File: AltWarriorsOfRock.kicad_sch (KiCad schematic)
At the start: 17 parts, among them J1 Fret Board, J2 South Inputs

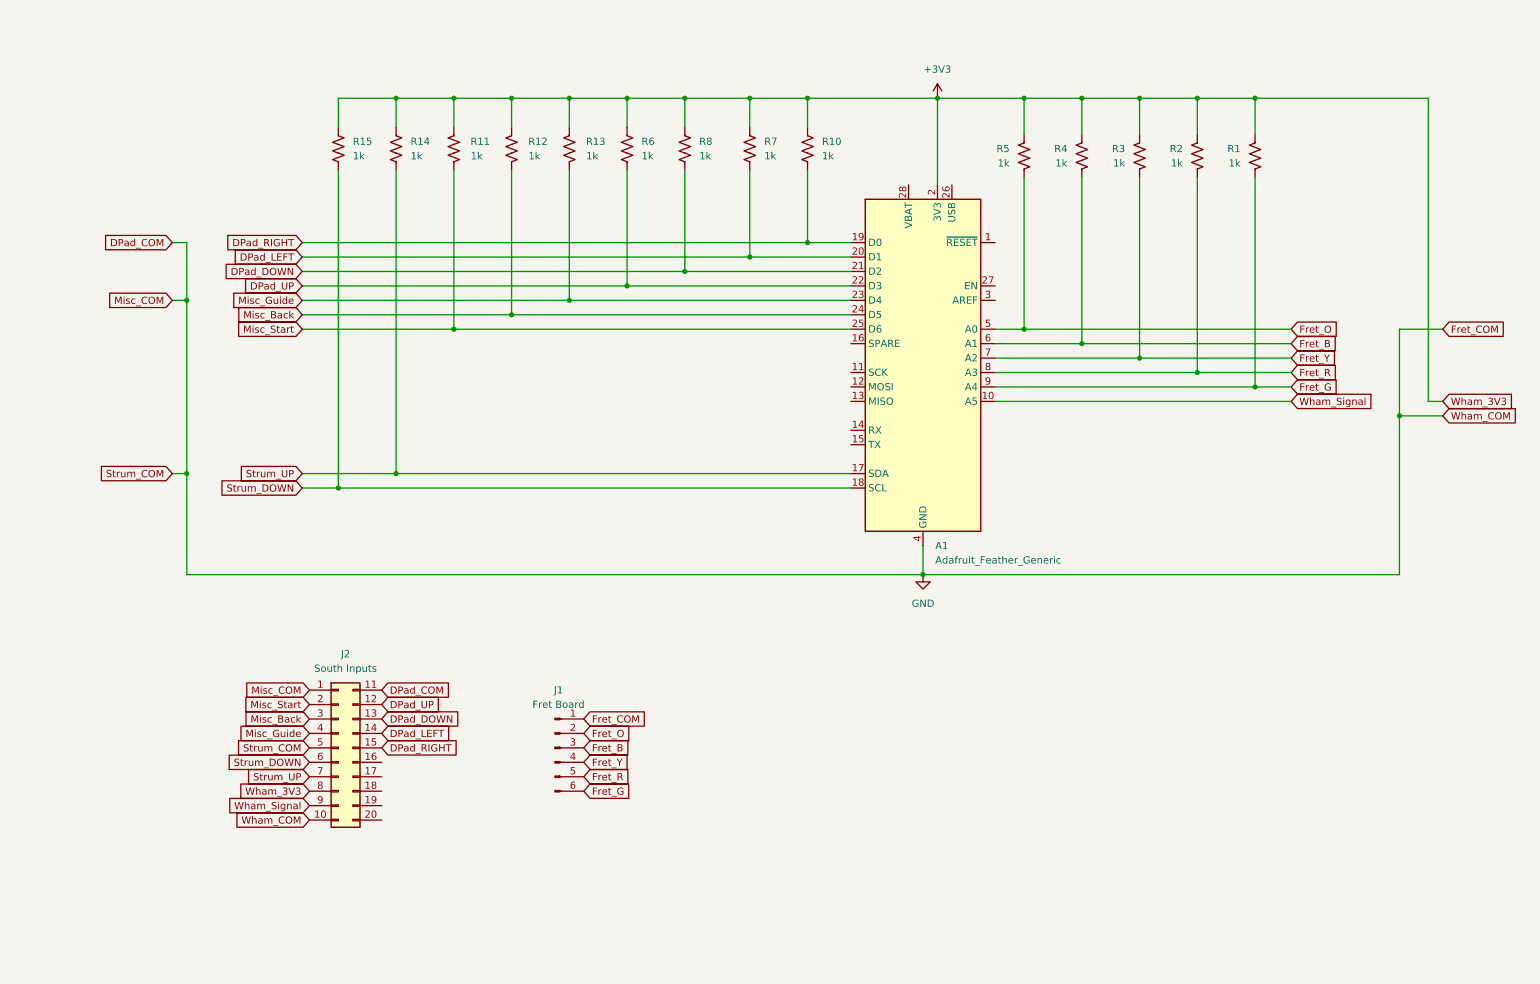
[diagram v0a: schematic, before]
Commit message: Switch to ESP32-S3-WROOM-1 module; Use 5.1k for all pullups
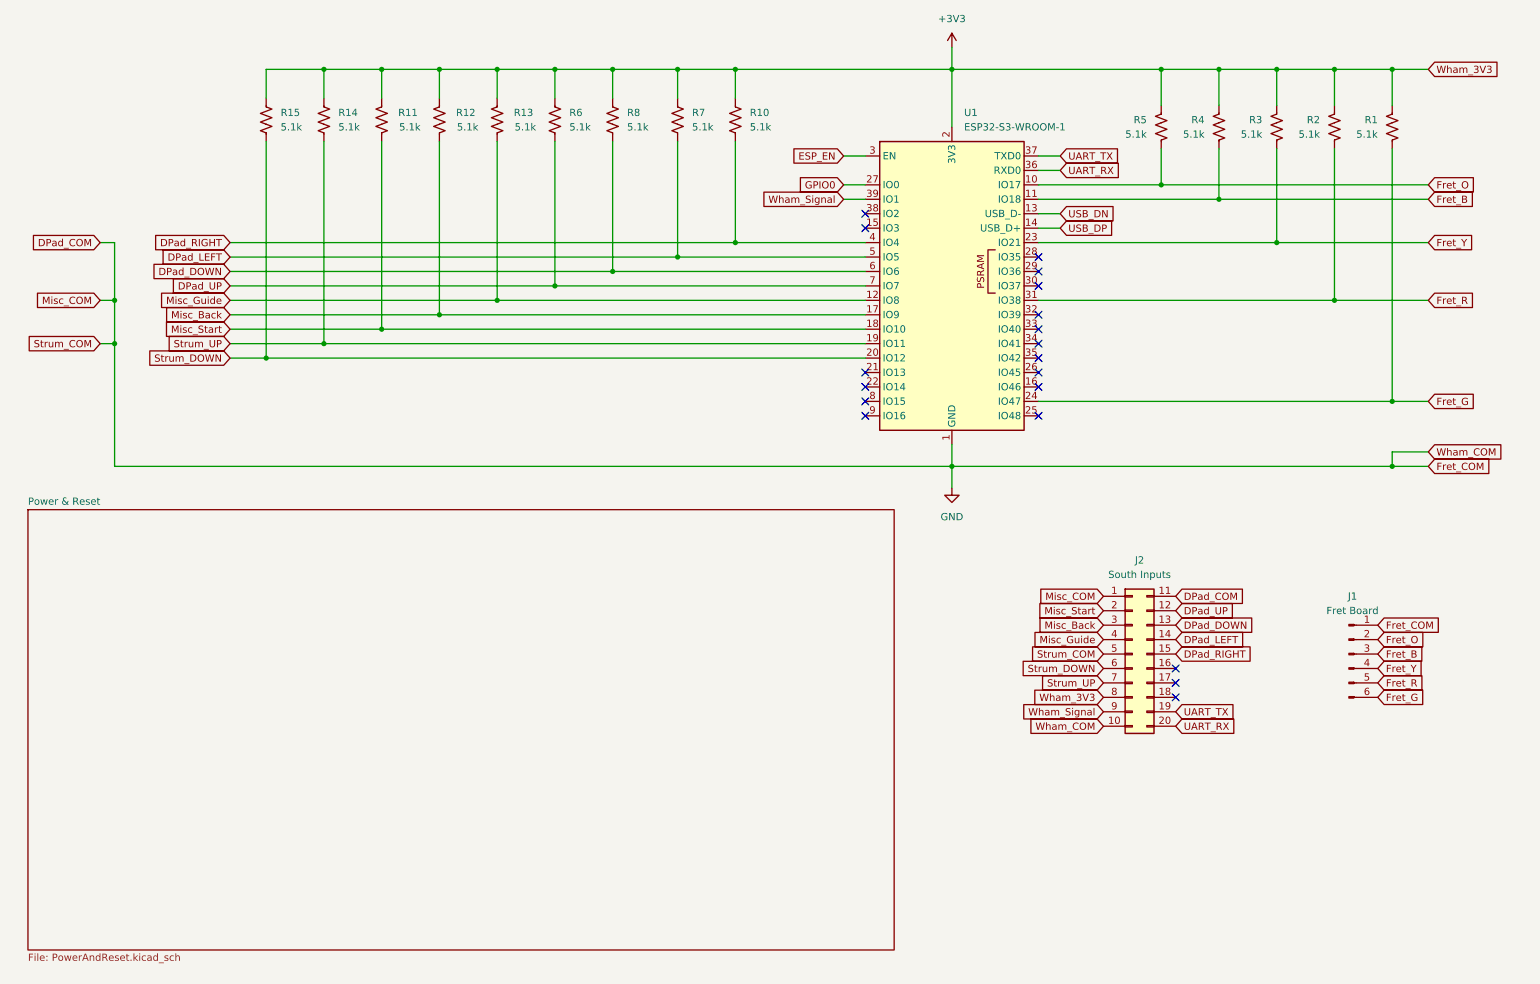
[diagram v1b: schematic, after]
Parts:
- removed A1: Adafruit_Feather_Generic, Module:Adafruit_Feather, symbol MCU_Module:Adafruit_Feather_Generic
- added U1: ESP32-S3-WROOM-1, RF_Module:ESP32-S3-WROOM-1, symbol RF_Module:ESP32-S3-WROOM-1
- R1, R10, R11, R12, R13, R14, R15, R2, R3, R4, R5, R6, R7, R8: value 1k -> 5.1k; footprint Resistor_THT:R_Axial_DIN0204_L3.6mm_D1.6mm_P7.62mm_Horizontal -> Resistor_SMD:R_1206_3216Metric_Pad1.30x1.75mm_HandSolder
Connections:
- net +3V3: now also U1.2 (3V3)
- net DPad_DOWN: now also U1.6 (IO6)
- net DPad_LEFT: now also U1.5 (IO5)
- net DPad_RIGHT: now also U1.4 (IO4)
- net DPad_UP: now also U1.7 (IO7)
- net Fret_B: now also U1.11 (IO18)
- net Fret_G: now also U1.24 (IO47)
- net Fret_O: now also U1.10 (IO17)
- net Fret_R: now also U1.31 (IO38)
- net Fret_Y: now also U1.23 (IO21)
- net GND: now also U1.1 (GND), U1.40 (GND), U1.41 (GND)
- net Misc_Back: now also U1.17 (IO9)
- net Misc_Guide: now also U1.12 (IO8)
- net Misc_Start: now also U1.18 (IO10)
- net Strum_DOWN: now also U1.20 (IO12)
- net Strum_UP: now also U1.19 (IO11)
- net Wham_Signal: now also U1.39 (IO1)
- net UART_TX: now reaches J2.19 (Pin_19)
- net UART_TX: now also U1.37 (TXD0)
- net UART_RX: now reaches J2.20 (Pin_20)
- net UART_RX: now also U1.36 (RXD0)
- new net ESP_EN: U1.3 (EN)
- new net GPIO0: U1.27 (IO0)
- new net USB_DN: U1.13 (USB_D-)
- new net USB_DP: U1.14 (USB_D+)
- no-connect marks 0 -> 19
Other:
- added sheet Power & Reset (PowerAndReset.kicad_sch)
- moved on the sheet: J1, J2, R1, R10, R11, R12, R13, R14, R15, R2, R3, R4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

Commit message: Draft 01 of PCB with WROOM module
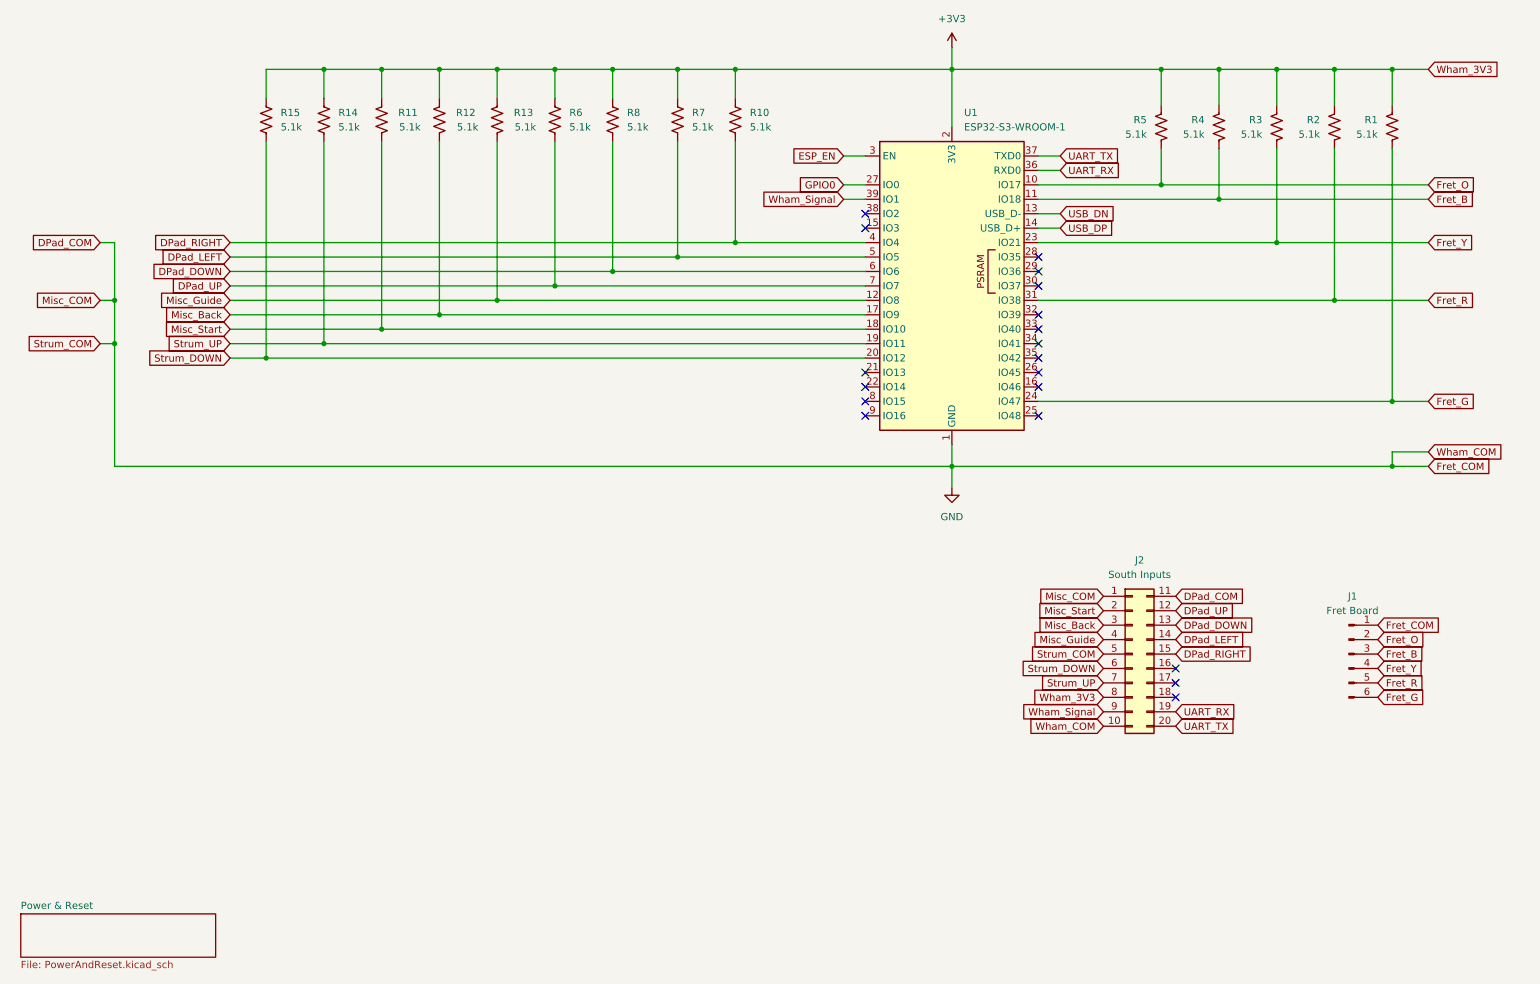
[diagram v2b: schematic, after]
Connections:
- net UART_RX: now also J2.19 (Pin_19); no longer J2.20 (Pin_20)
- net UART_TX: now also J2.20 (Pin_20); no longer J2.19 (Pin_19)
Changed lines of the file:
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@@
 	(global_label "UART_RX"
 		(shape input)
+		(at 219.71 148.59 0)
+		(fields_autoplaced yes)
+		(effects
+			(font
+				(size 1.27 1.27)
+			)
+			(justify left)
+		)
+		(property "Intersheetrefs" "${INTERSHEET_REFS}"
+			(at 230.799 148.59 0)
+			(effects
+				(font
+					(size 1.27 1.27)
+				)
+				(justify left)
+				(hide yes)
+			)
+		)
+	)
+	(global_label "DPad_RIGHT"
+		(shape input)
+		(at 53.34 66.04 180)
+		(fields_autoplaced yes)
+		(effects
+			(font
+				(size 1.27 1.27)
+			)
+			(justify right)
+		)
+		(property "Intersheetrefs" "${INTERSHEET_REFS}"
+			(at 39.1063 66.04 0)
+			(effects
+				(font
+					(size 1.27 1.27)
+				)
+				(justify right)
+				(hide yes)
+			)
+		)
+	)
+	(global_label "Fret_B"
+		(shape input)
+		(at 264.16 58.42 0)
+		(fields_autoplaced yes)
+		(effects
+			(font
+				(size 1.27 1.27)
+			)
+			(justify left)
+		)
+		(property "Intersheetrefs" "${INTERSHEET_REFS}"
+			(at 273.0719 58.42 0)
+			(effects
+				(font
+					(size 1.27 1.27)
+				)
+				(justify left)
+				(hide yes)
+			)
+		)
+	)
+	(global_label "Fret_G"
+		(shape input)
+		(at 255.27 146.05 0)
+		(fields_autoplaced yes)
+		(effects
+			(font
+				(size 1.27 1.27)
+			)
+			(justify left)
+		)
+		(property "Intersheetrefs" "${INTERSHEET_REFS}"
+			(at 264.1819 146.05 0)
+			(effects
+				(font
+					(size 1.27 1.27)
+				)
+				(justify left)
+				(hide yes)
+			)
+		)
+	)
+	(global_label "UART_TX"
+		(shape input)
 		(at 219.71 151.13 0)
 		(fields_autoplaced yes)
@@
 		)
 		(property "Intersheetrefs" "${INTERSHEET_REFS}"
-			(at 230.799 151.13 0)
-			(effects
-				(font
-					(size 1.27 1.27)
-				)
-				(justify left)
-				(hide yes)
-			)
-		)
-	)
-	(global_label "DPad_RIGHT"
-		(shape input)
-		(at 53.34 66.04 180)
-		(fields_autoplaced yes)
-		(effects
-			(font
-				(size 1.27 1.27)
-			)
-			(justify right)
-		)
-		(property "Intersheetrefs" "${INTERSHEET_REFS}"
-			(at 39.1063 66.04 0)
-			(effects
-				(font
-					(size 1.27 1.27)
-				)
-				(justify right)
-				(hide yes)
-			)
-		)
-	)
-	(global_label "Fret_B"
-		(shape input)
-		(at 264.16 58.42 0)
-		(fields_autoplaced yes)
-		(effects
-			(font
-				(size 1.27 1.27)
-			)
-			(justify left)
-		)
-		(property "Intersheetrefs" "${INTERSHEET_REFS}"
-			(at 273.0719 58.42 0)
-			(effects
-				(font
-					(size 1.27 1.27)
-				)
-				(justify left)
-				(hide yes)
-			)
-		)
-	)
-	(global_label "Fret_G"
-		(shape input)
-		(at 255.27 146.05 0)
-		(fields_autoplaced yes)
-		(effects
-			(font
-				(size 1.27 1.27)
-			)
-			(justify left)
-		)
-		(property "Intersheetrefs" "${INTERSHEET_REFS}"
-			(at 264.1819 146.05 0)
-			(effects
-				(font
-					(size 1.27 1.27)
-				)
-				(justify left)
-				(hide yes)
-			)
-		)
-	)
-	(global_label "UART_TX"
-		(shape input)
-		(at 219.71 148.59 0)
-		(fields_autoplaced yes)
-		(effects
-			(font
-				(size 1.27 1.27)
-			)
-			(justify left)
-		)
-		(property "Intersheetrefs" "${INTERSHEET_REFS}"
-			(at 230.4966 148.59 0)
+			(at 230.4966 151.13 0)
 			(effects
 				(font
@@
 	)
 	(sheet
-		(at 17.78 113.03)
-		(size 152.4 77.47)
+		(at 16.51 184.15)
+		(size 34.29 7.62)
 		(exclude_from_sim no)
 		(in_bom yes)
@@
 		)
 		(property "Sheetname" "Power & Reset"
-			(at 17.78 112.3184 0)
+			(at 16.51 183.4384 0)
 			(effects
 				(font
@@
 		)
 		(property "Sheetfile" "PowerAndReset.kicad_sch"
-			(at 17.78 191.0846 0)
-			(effects
-				(font
+			(at 16.51 192.3546 0)
+			(effects
+				(font

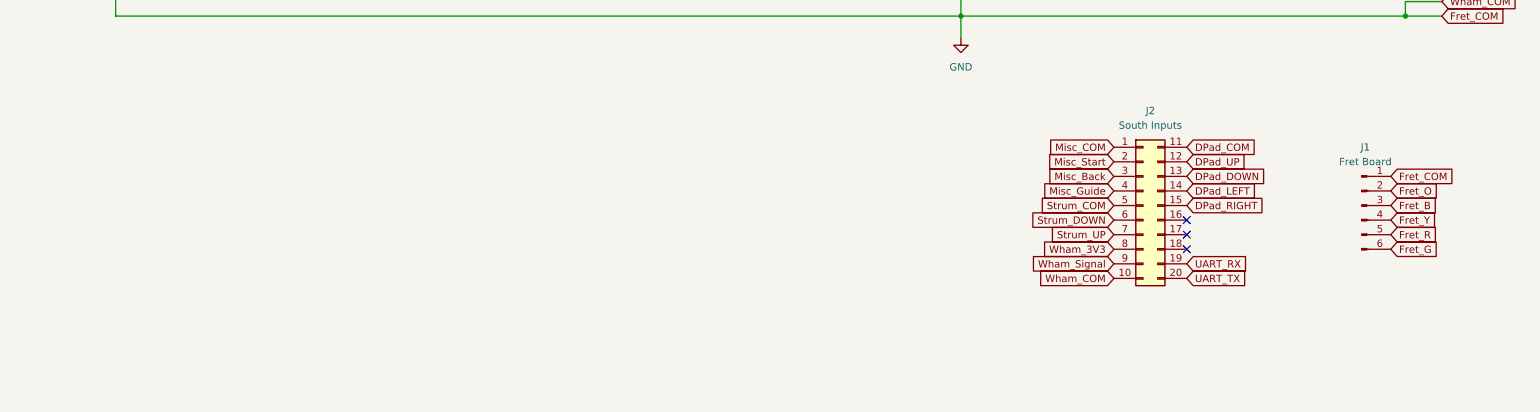
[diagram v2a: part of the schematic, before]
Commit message: [WIP] Use surface-mount headers for south headers
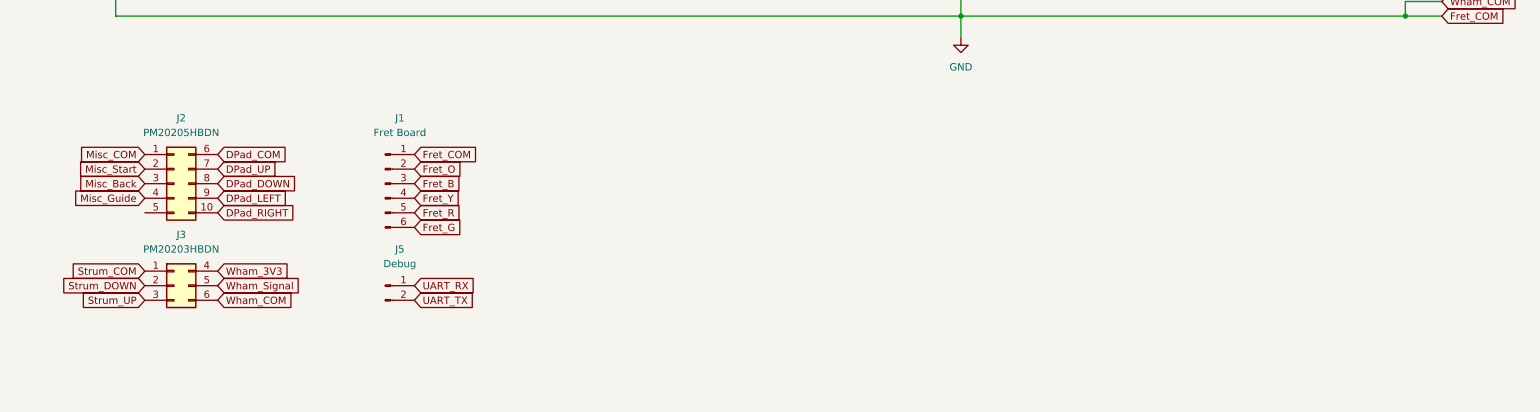
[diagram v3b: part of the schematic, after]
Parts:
- removed J2: South Inputs, Library_ygaskh:PinHeader_2x10_P2.54mm_Vertical_TopBottom, symbol Connector_Generic:Conn_02x10_Top_Bottom
- added J2: PM20205HBDN, Connector_Metz_ygaskh:PM20205HBDN, symbol Connector_Metz:PM20205HBDN
- added J3: PM20203HBDN, Connector_Metz_ygaskh:PM20203HBDN, symbol Connector_Metz:PM20203HBDN
- added J5: Debug, Connector_PinHeader_2.54mm:PinHeader_1x02_P2.54mm_Vertical, symbol Connector:Conn_01x02_Pin
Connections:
- net +3V3: now also J3.4 (Pin_4)
- net DPad_DOWN: now also J2.8 (Pin_8)
- net DPad_LEFT: now also J2.9 (Pin_9)
- net DPad_RIGHT: now also J2.10 (Pin_10)
- net DPad_UP: now also J2.7 (Pin_7)
- net GND: now also J2.1 (Pin_1), J2.6 (Pin_6), J3.1 (Pin_1), J3.6 (Pin_6)
- net Misc_Back: now also J2.3 (Pin_3)
- net Misc_Guide: now also J2.4 (Pin_4)
- net Misc_Start: now also J2.2 (Pin_2)
- net Strum_DOWN: now also J3.2 (Pin_2)
- net Strum_UP: now also J3.3 (Pin_3)
- net UART_RX: now also J5.1 (Pin_1)
- net UART_TX: now also J5.2 (Pin_2)
- net Wham_Signal: now also J3.5 (Pin_5)
- no-connect marks 19 -> 16
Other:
- moved on the sheet: J1

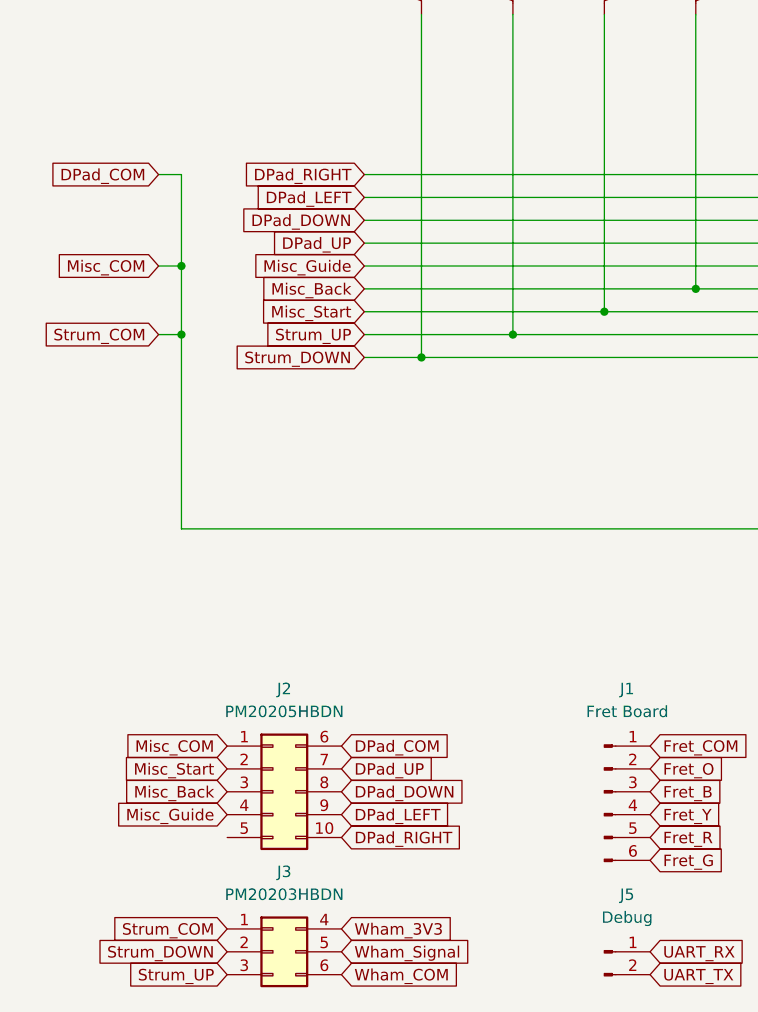
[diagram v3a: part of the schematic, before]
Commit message: Redo layout with USB-C port on the underside
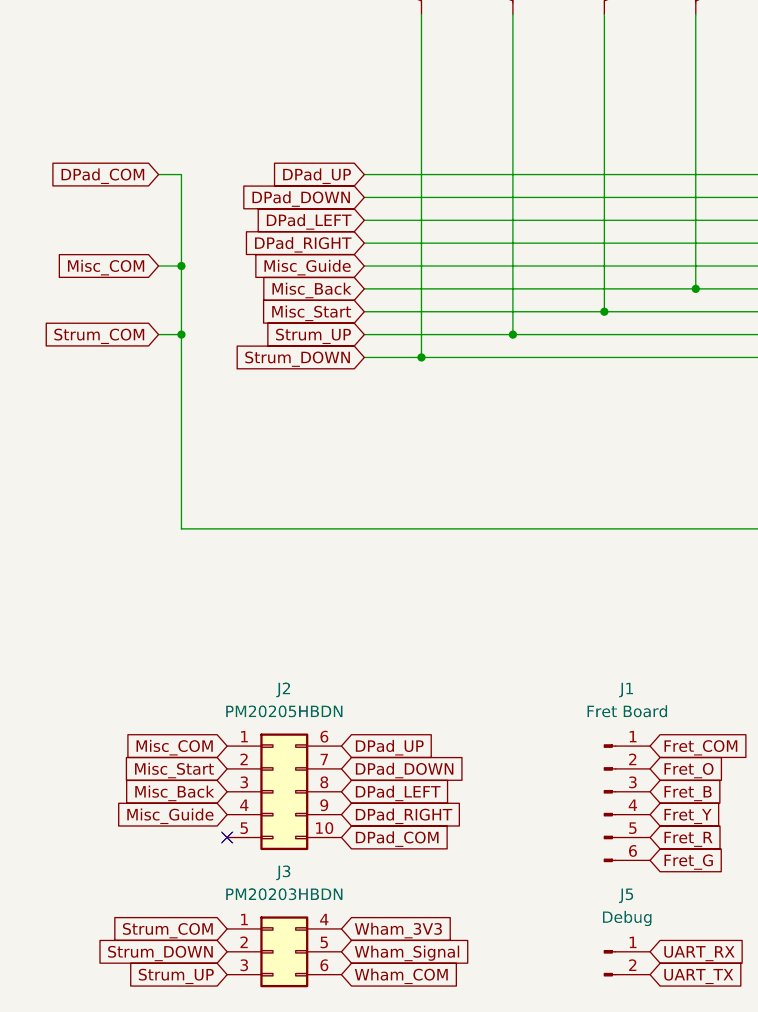
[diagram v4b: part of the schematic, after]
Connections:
- net DPad_DOWN: now also J2.7 (Pin_7), R7.2, U1.5 (IO5); no longer J2.8 (Pin_8), R8.2, U1.6 (IO6)
- net DPad_LEFT: now also J2.8 (Pin_8), R8.2, U1.6 (IO6); no longer J2.9 (Pin_9), R7.2, U1.5 (IO5)
- net DPad_RIGHT: now also J2.9 (Pin_9), R6.2, U1.7 (IO7); no longer J2.10 (Pin_10), R10.2, U1.4 (IO4)
- net DPad_UP: now also J2.6 (Pin_6), R10.2, U1.4 (IO4); no longer J2.7 (Pin_7), R6.2, U1.7 (IO7)
- net GND: now also J2.10 (Pin_10); no longer J2.6 (Pin_6)
- no-connect marks 16 -> 17
